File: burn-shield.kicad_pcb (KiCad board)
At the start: 2 copper layers, 3 parts, among them J1 28 ZIF Socket

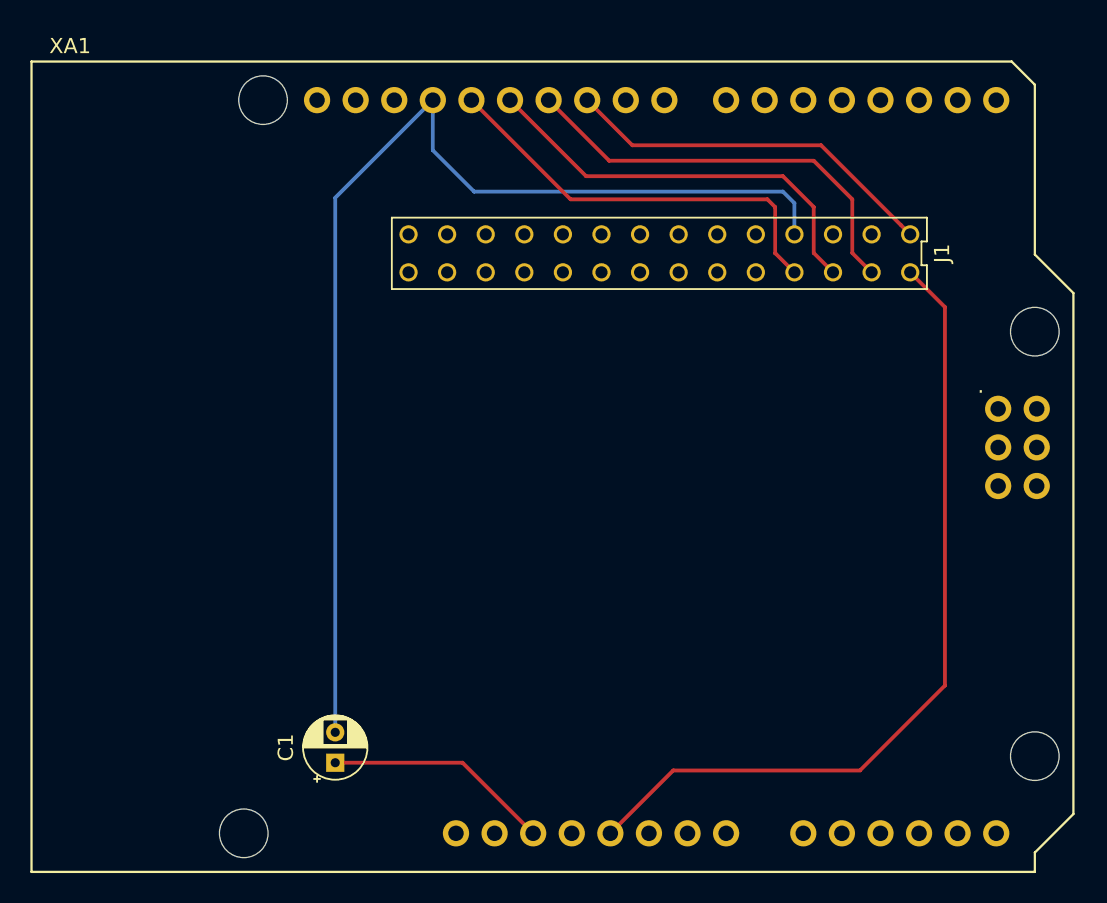
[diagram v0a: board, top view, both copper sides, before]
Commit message: Added the ATMEGA support too
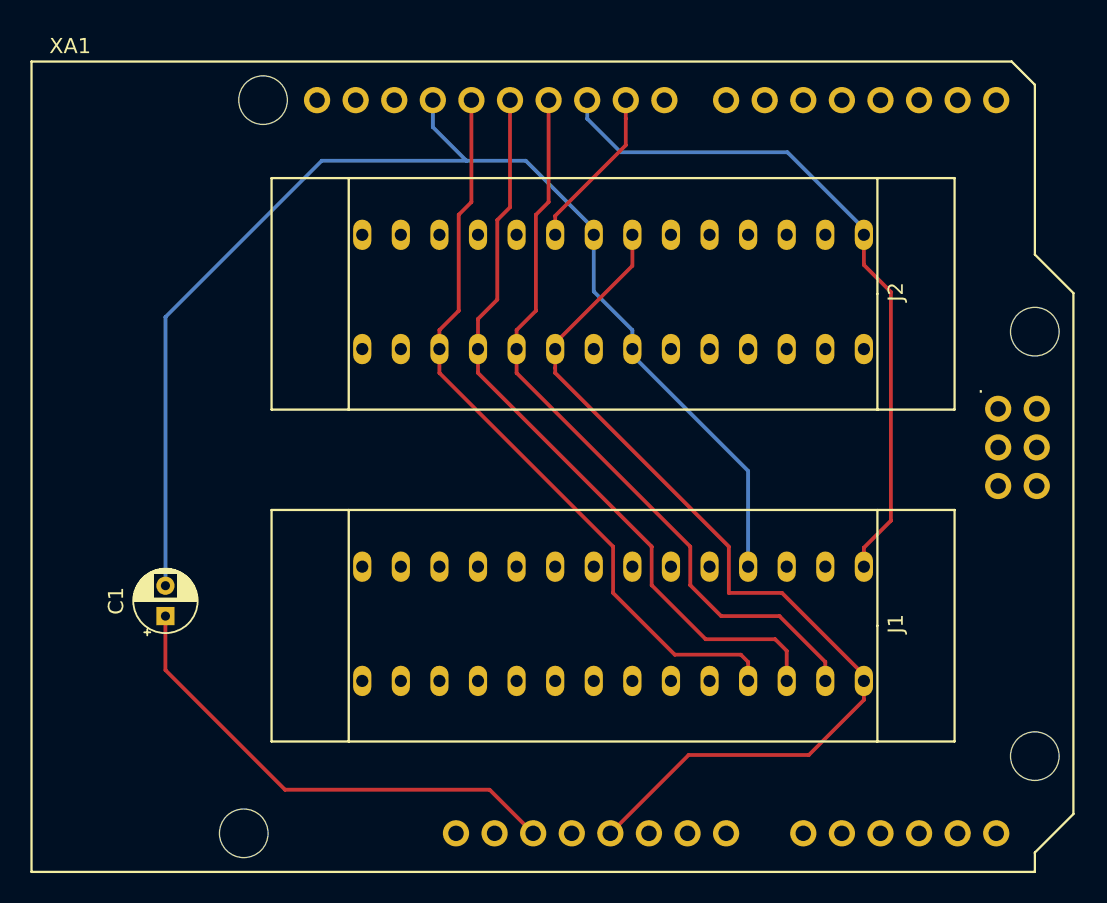
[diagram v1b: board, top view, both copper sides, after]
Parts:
- added J2: 28 ZIF Socket - ATMEGA328, ZIF:DIP-28_296_ELL, F.Cu at (130.0, 91.9)
- J1: value 28 ZIF Socket -> 28 ZIF Socket - ATTiny; footprint ZIF:ZIF-DIP-28_98 -> ZIF:DIP-28_296_ELL
- moved J1 24.6 mm to (130.0, 113.8)
- moved C1 14.8 mm to (100.6, 113.3)
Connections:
- XA1 pad D9: Net-(XA1-PadD9) -> /Pin9X
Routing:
- net /Pin12: track 27.7 -> 50.2 mm
- net /Pin11: track 27.7 -> 50.1 mm
- net /Pin13: track 28.0 -> 49.8 mm
- net /Pin10: track 24.9 -> 46.6 mm
- net Net-(C1-Pad1): track 15.0 -> 32.2 mm
- net /Pin9X: track 0.00 -> 10.8 mm
- net VCC: track 54.2 -> 63.5 mm
- net GND: track 74.9 -> 83.3 mm

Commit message: Updated the pcb
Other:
- board outline added: 68.6 x 53.3 mm
- board text added: "Burn Board v0.2 Krishna"
- board text added: "TINY"
